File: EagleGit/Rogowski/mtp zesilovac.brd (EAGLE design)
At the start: 160 x 100 mm, 25 parts, among them IC1 TL061P, IC2 TL061P, IC3 TL061P, X1 SMKDSP_1,5/2, X2 SMKDSP_1,5/2, X3 SMKDSP_1,5/2, X4 SMKDSP_1,5/2, X5 SMKDSP_1,5/2, X6 SMKDSP_1,5/2, X7 SMKDSP_1,5/2

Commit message: DPS pro akvarko
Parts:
- added U$1, U$2, U$3, U$4: (no value), holes:3,2
- R2, R5, R8: device pot:SP19L -> pot:LI10
- moved R2 30.5 mm to (57.1, 17.8), turned to 180 degrees
- moved R5 29.6 mm to (87.6, 17.8), turned to 180 degrees
- moved R8 29.3 mm to (118.1, 17.8), turned to 180 degrees
- moved IC4 28.0 mm to (14.0, 11.4)
- moved C1 28.0 mm to (14.0, 19.1)
- moved C2 28.0 mm to (14.6, 5.08)
- moved C5 28.0 mm to (24.1, 6.35)
- moved C3 28.0 mm to (21.6, 27.9)
- moved C4 28.0 mm to (24.1, 15.2)
- moved X7 28.0 mm to (12.7, 38.1)
- moved R1 25.7 mm to (34.3, 24.1)
- moved X1 24.4 mm to (43.2, 6.35)
- moved IC1 24.4 mm to (44.5, 24.1)
- moved R3 24.4 mm to (43.2, 15.2)
- moved X2 24.4 mm to (43.2, 38.1)
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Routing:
- net GND: track 82.8 -> 99.8 mm
- net N$12: track 25.4 -> 15.8 mm
- net N$8: track 25.4 -> 15.8 mm
- net N$4: track 25.4 -> 15.8 mm
- net N$7: track 8.94 -> 13.5 mm
- net N$11: track 8.94 -> 13.5 mm
- net N$3: track 8.94 -> 13.5 mm
- net N$1: track 20.9 -> 23.3 mm
- net N$9: track 21.2 -> 23.3 mm
- net N$5: track 21.2 -> 23.3 mm
- net N$6: track 23.7 -> 25.5 mm
- net N$2: track 23.7 -> 25.5 mm
- net N$10: track 26.2 -> 28.0 mm
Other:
- board size 160 x 100 mm -> 129.5 x 44.1 mm

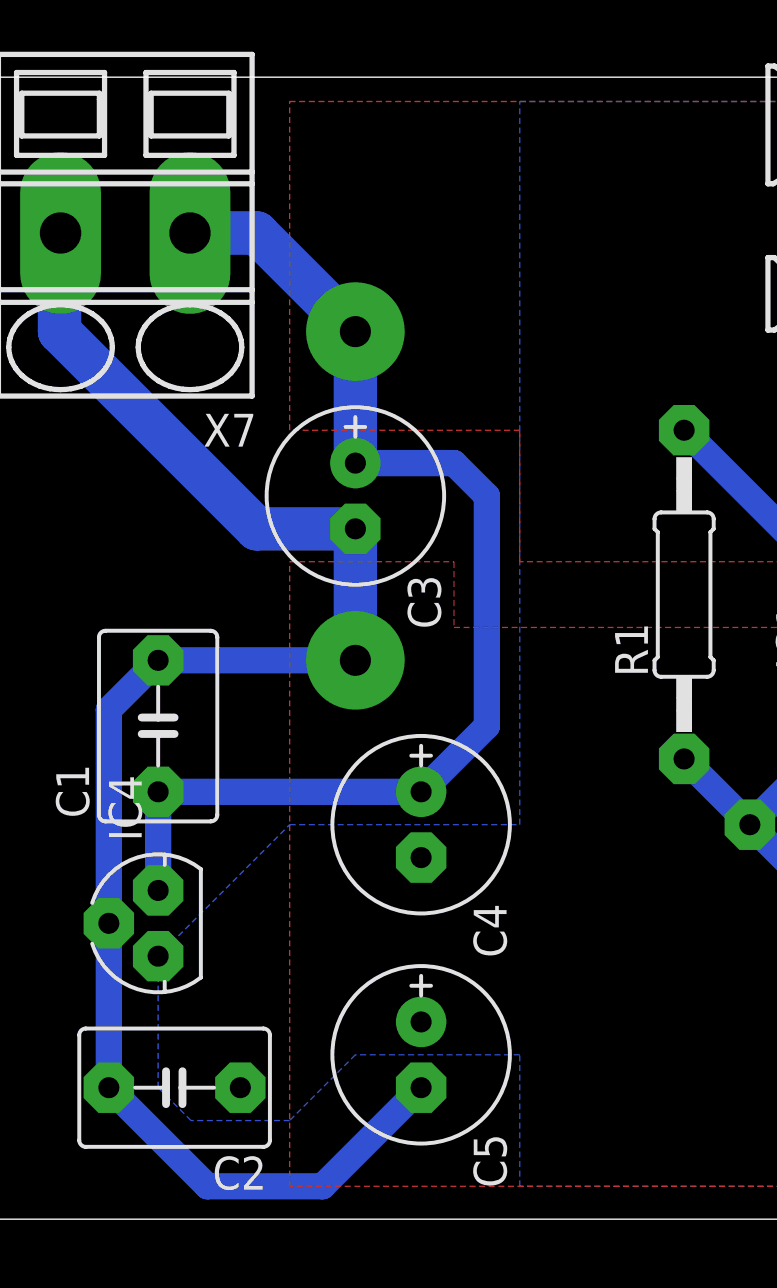
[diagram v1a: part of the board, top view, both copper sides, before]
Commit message: Vytvorena cela pro Rogowskiho civku a dodelan budic LED
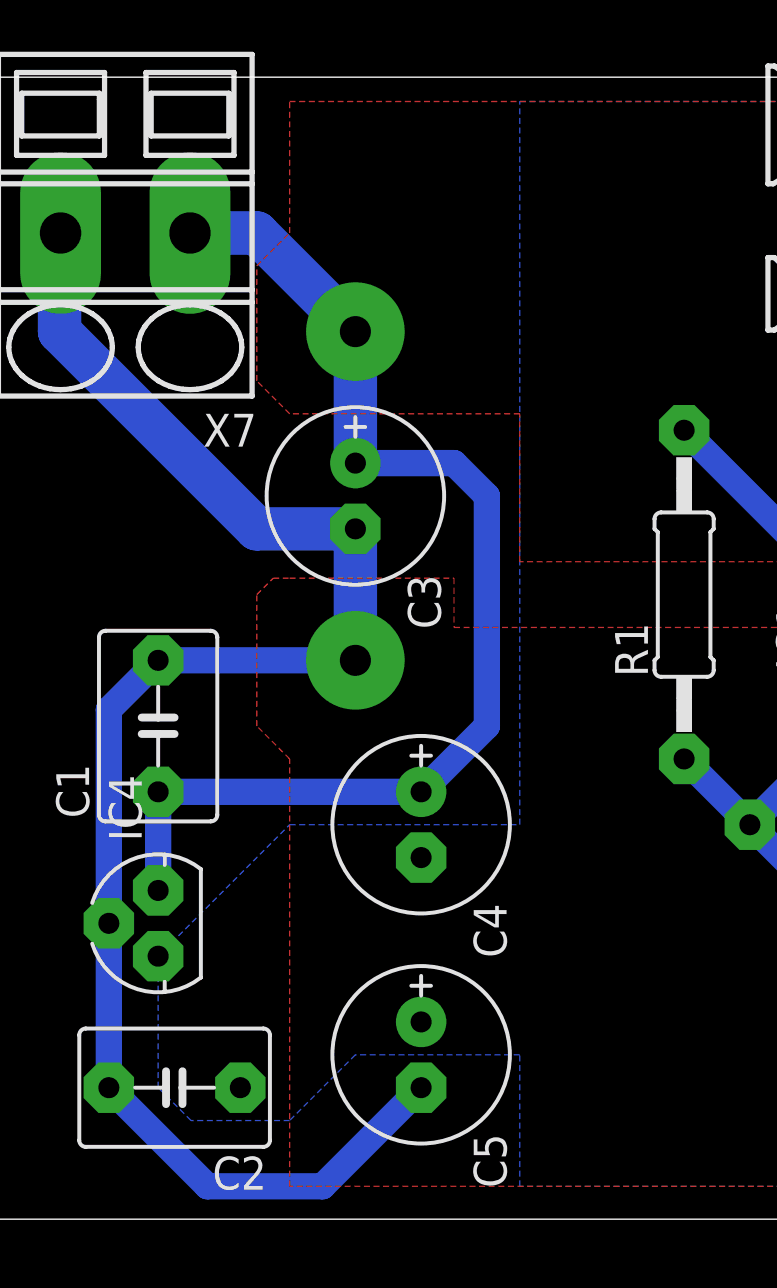
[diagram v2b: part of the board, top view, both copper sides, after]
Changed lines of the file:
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@@
 <wire x1="21.59" y1="21.59" x2="21.59" y2="26.67" width="1.6764" layer="16"/>
 <polygon width="0.4064" layer="1">
-<vertex x="19.05" y="25.4"/>
-<vertex x="25.4" y="25.4"/>
+<vertex x="19.05" y="24.765"/>
+<vertex x="25.4" y="24.765"/>
 <vertex x="25.4" y="22.86"/>
 <vertex x="121.92" y="22.86"/>
 <vertex x="121.92" y="1.27"/>
 <vertex x="19.05" y="1.27"/>
+<vertex x="19.05" y="17.78"/>
+<vertex x="17.78" y="19.05"/>
+<vertex x="17.78" y="24.13"/>
+<vertex x="18.415" y="24.765"/>
 </polygon>
 <via x="21.59" y="21.59" extent="1-16" drill="1.2" diameter="3.81"/>
@@
 <wire x1="21.59" y1="34.29" x2="21.59" y2="29.21" width="1.6764" layer="16"/>
 <polygon width="0.4064" layer="1">
-<vertex x="19.05" y="30.48"/>
+<vertex x="19.05" y="31.115"/>
+<vertex x="17.78" y="32.385"/>
+<vertex x="17.78" y="36.83"/>
+<vertex x="19.05" y="38.1"/>
 <vertex x="19.05" y="43.18"/>
 <vertex x="121.92" y="43.18"/>
 <vertex x="121.92" y="25.4"/>
 <vertex x="27.94" y="25.4"/>
-<vertex x="27.94" y="30.48"/>
+<vertex x="27.94" y="31.115"/>
 </polygon>
 <via x="21.59" y="34.29" extent="1-16" drill="1.2" diameter="3.81"/>
